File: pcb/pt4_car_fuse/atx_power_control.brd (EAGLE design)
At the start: 86 x 70 mm, 61 parts, among them IC2 REG1117, IC3 STM32F042F4, IC4 MY_7905DT, J1 ATX24RH, SW1 324_SW, SW2 324_SW, SW3 324_SW, SW4 324_SW, SW5 324_SW, SW7 324_SW, U1 USBC_16P, U2 USBC_16P

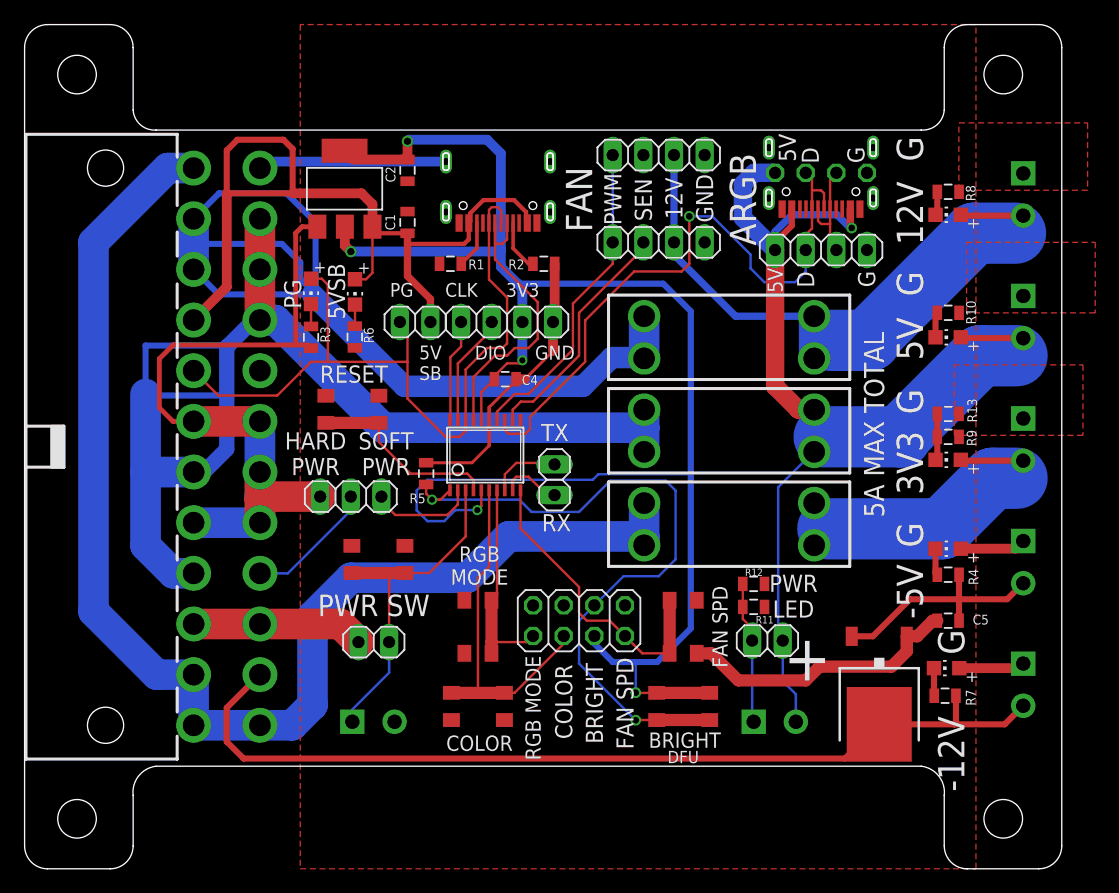
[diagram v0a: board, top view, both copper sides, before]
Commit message: fixed fuse holder footprint
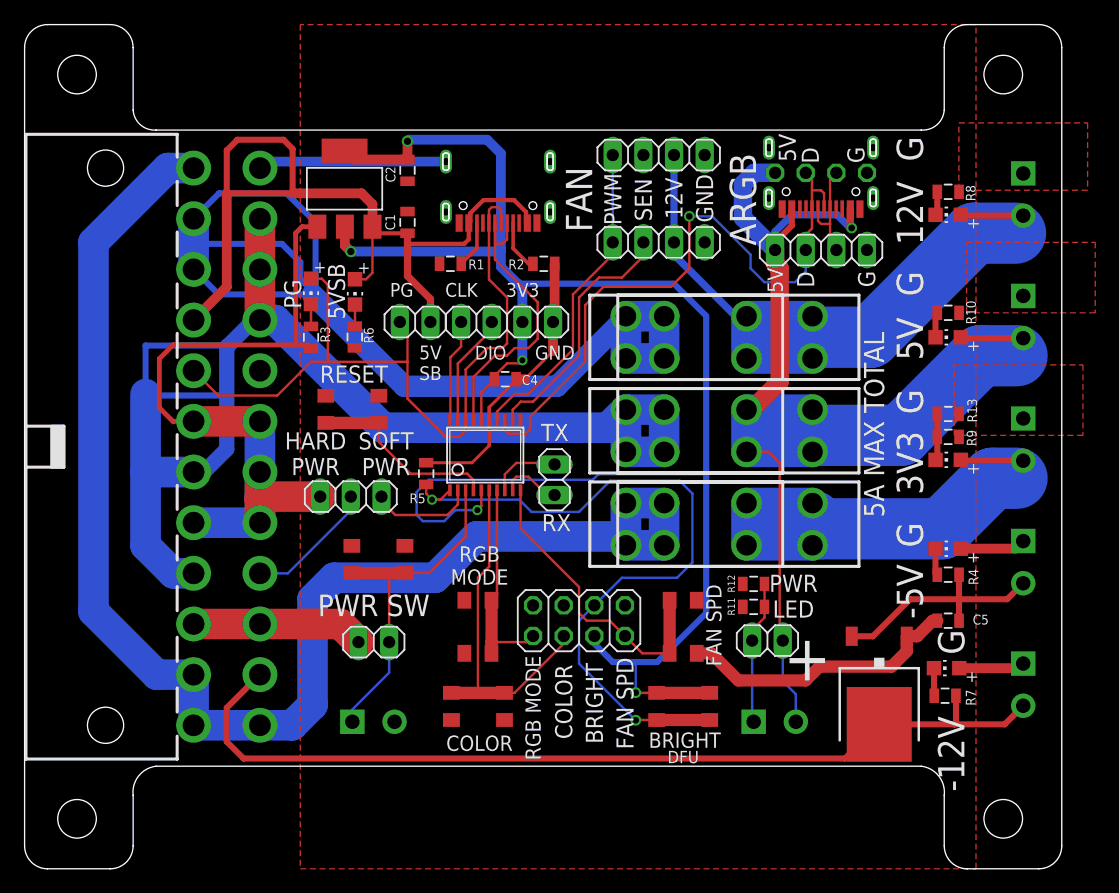
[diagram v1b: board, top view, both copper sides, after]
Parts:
- added U$4, U$6, U$9: FUSE_HOLDER, atx_power_control:FUSE_HOLDER_MINI_ONLY
- moved U$5 0.76 mm to (59.2, 44.1)
- moved U$7 0.76 mm to (59.2, 28.6)
- moved U$8 0.76 mm to (59.2, 36.3)
- turned R11 to 0 degrees
- turned R12 to 0 degrees
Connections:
- net N$10: now also U$9.A0, U$9.A1
- net N$14: now also U$6.A0, U$6.A1
- net N$15: now also U$4.B0, U$4.B1
- net N$16: now also U$6.B0, U$6.B1
- net N$21: now also U$4.A0, U$4.A1
- net N$30: now also U$9.B0, U$9.B1
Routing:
- net N$16: track 29.6 -> 50.1 mm
- net N$30: track 94.5 -> 114.9 mm
- net N$15: track 53.7 -> 66.6 mm
- net N$21: track 81.0 -> 90.7 mm
- net N$14: track 107.8 -> 117.2 mm
- net N$10: track 102.3 -> 111.3 mm
- net +3V3: track 148.2 -> 151.1 mm
- net BUTTON2: track 57.5 -> 60.3 mm
- net N$6: track 19.8 -> 20.9 mm
- net N$35: track 52.6 -> 53.6 mm
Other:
- board text added: "ATX4VC.com dekuNukem SEPT 2022 PT4"
- board text removed: "ATX4VC.com dekuNukem SEPT 2022 PT5"
